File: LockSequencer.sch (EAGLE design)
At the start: 78 parts, among them IC1 4017D, IC2 NE555, K1 G2RATE-OJ, K2 G2RATE-OJ

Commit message: Nearly completed second revision
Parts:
- removed H2: MOUNT-HOLE2.8, holes:MOUNT-HOLE2.8
- added H3: MOUNT-PAD-ROUND2.8, holes:MOUNT-PAD-ROUND2.8
- H1: value MOUNT-HOLE2.8 -> MOUNT-PAD-ROUND2.8; device holes:MOUNT-HOLE2.8 -> holes:MOUNT-PAD-ROUND2.8
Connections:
- net N$27: now also K11.1; no longer K11.2
- net VSUPPLY: now also K11.2; no longer K11.1
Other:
- moved on the sheet: H1, K1
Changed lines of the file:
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@@
 <part name="JP7" library="pinhead" deviceset="PINHD-1X2" device=""/>
 <part name="JP8" library="pinhead" deviceset="PINHD-1X2" device=""/>
-<part name="H1" library="holes" deviceset="MOUNT-HOLE" device="2.8" value="MOUNT-HOLE2.8"/>
-<part name="H2" library="holes" deviceset="MOUNT-HOLE" device="2.8" value="MOUNT-HOLE2.8"/>
+<part name="H3" library="holes" deviceset="MOUNT-PAD-ROUND" device="2.8"/>
+<part name="H1" library="holes" deviceset="MOUNT-PAD-ROUND" device="2.8"/>
 </parts>
 <sheets>
@@
 <instance part="R4" gate="G$1" x="203.2" y="167.64" rot="R90"/>
 <instance part="T1" gate="G$1" x="223.52" y="20.32"/>
-<instance part="K1" gate="1" x="330.2" y="114.3"/>
+<instance part="K1" gate="1" x="330.2" y="114.3" rot="R180"/>
 <instance part="K1" gate="2" x="342.9" y="129.54"/>
 <instance part="D6" gate="G$1" x="378.46" y="127" rot="R180"/>
@@
 <instance part="JP7" gate="G$1" x="251.46" y="53.34" rot="R180"/>
 <instance part="JP8" gate="G$1" x="251.46" y="45.72" rot="R180"/>
-<instance part="H1" gate="G$1" x="302.26" y="165.1"/>
-<instance part="H2" gate="G$1" x="330.2" y="165.1"/>
+<instance part="H3" gate="G$1" x="309.88" y="175.26"/>
+<instance part="H1" gate="G$1" x="309.88" y="167.64"/>
 </instances>
 <busses>
@@
 </segment>
 <segment>
-<pinref part="K1" gate="1" pin="1"/>
-<wire x1="330.2" y1="127" x2="330.2" y2="119.38" width="0.1524" layer="91"/>
 <wire x1="330.2" y1="127" x2="320.04" y2="127" width="0.1524" layer="91"/>
 <pinref part="D1" gate="1" pin="2"/>
@@
 <wire x1="312.42" y1="124.46" x2="312.42" y2="127" width="0.1524" layer="91"/>
 <junction x="312.42" y="127"/>
+<pinref part="K1" gate="1" pin="2"/>
+<wire x1="330.2" y1="119.38" x2="330.2" y2="127" width="0.1524" layer="91"/>
 </segment>
 </net>
@@
 </segment>
 </net>
-<net name="VDD" class="1">
+<net name="VDD" class="3">
 <segment>
 <pinref part="R6" gate="G$1" pin="2"/>
@@
 <pinref part="T4" gate="G$1" pin="C"/>
 <wire x1="312.42" y1="99.06" x2="312.42" y2="101.6" width="0.1524" layer="91"/>
-<pinref part="K1" gate="1" pin="2"/>
-<wire x1="330.2" y1="109.22" x2="330.2" y2="101.6" width="0.1524" layer="91"/>
 <wire x1="330.2" y1="101.6" x2="320.04" y2="101.6" width="0.1524" layer="91"/>
 <pinref part="D1" gate="1" pin="1"/>
@@
 <wire x1="312.42" y1="104.14" x2="312.42" y2="101.6" width="0.1524" layer="91"/>
 <junction x="312.42" y="101.6"/>
-</segment>
-</net>
+<pinref part="K1" gate="1" pin="1"/>
+<wire x1="330.2" y1="109.22" x2="330.2" y2="101.6" width="0.1524" layer="91"/>
+</segment>
+</net>

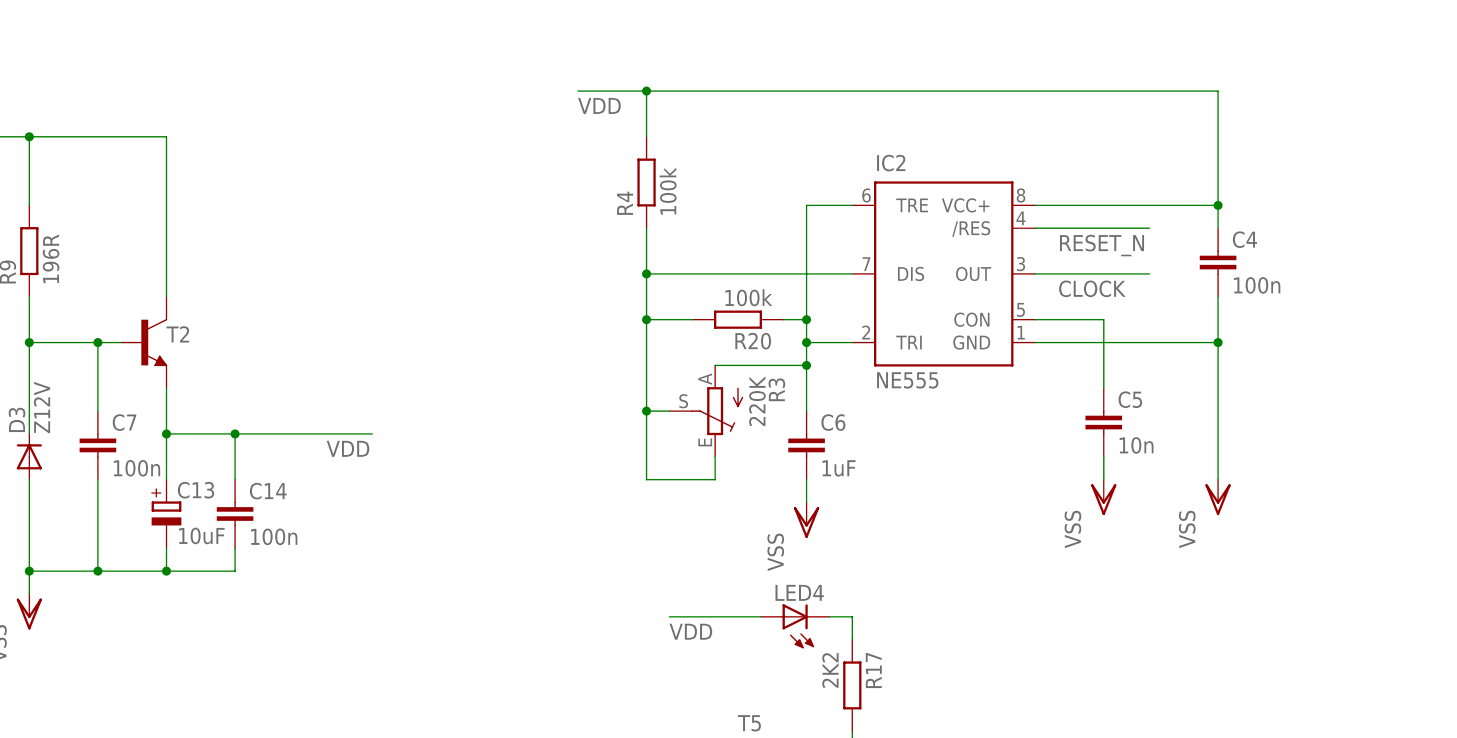
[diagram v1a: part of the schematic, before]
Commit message: Nearly finished on second revision - ground and power resrouted on right side of board. 4017 and 55 nearly done.
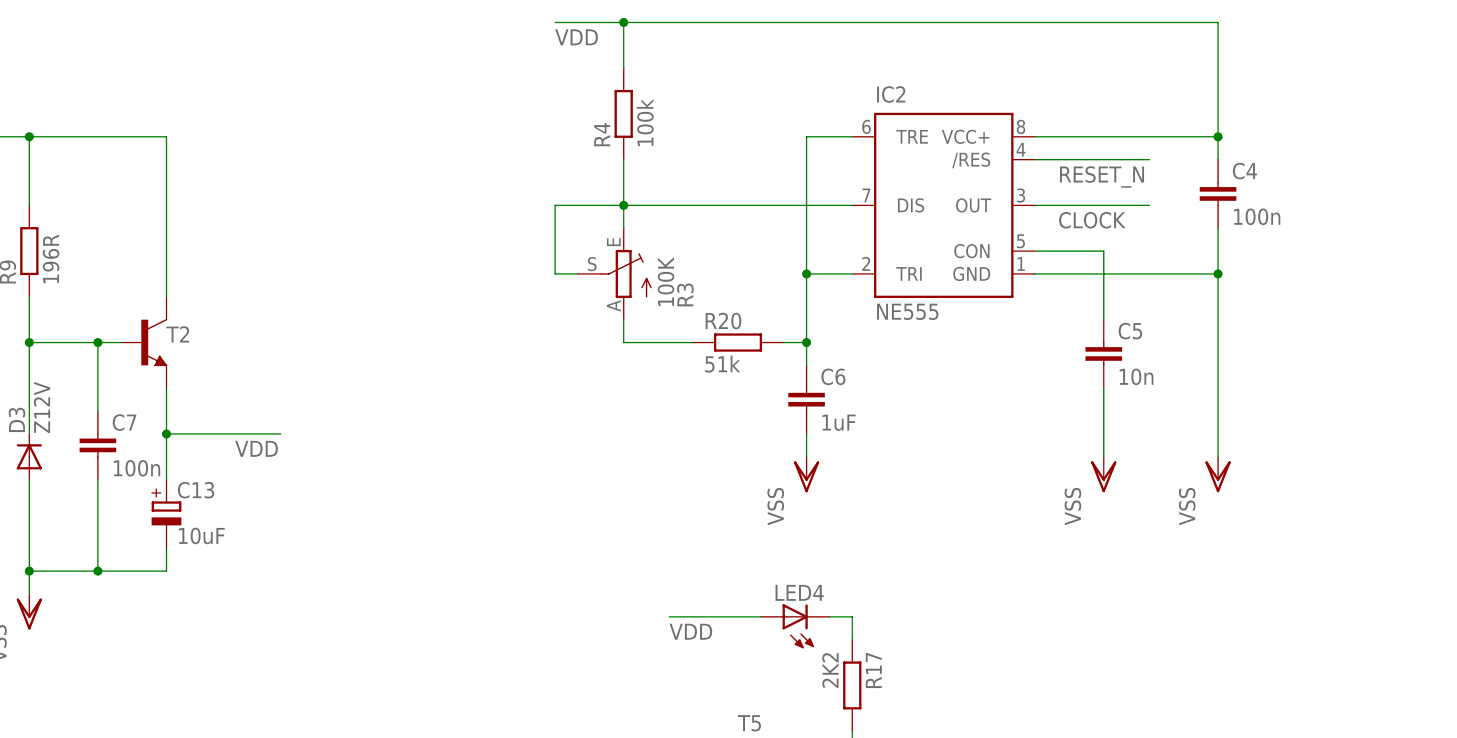
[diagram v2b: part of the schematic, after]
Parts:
- removed C14: 100n, rcl:C-EU050-024X044
- R17: device rcl:R-EU_0309/12 -> rcl:R-EU_0207/7
- R20: value 100k -> 51k
- R3: value 220K -> 100K
- R8: device rcl:R-EU_R0402 -> rcl:R-EU_0207/7
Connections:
- removed net N$24: IC2.DIS, R20.2, R3.E, R3.S, R4.1
- new net N$29: IC2.DIS, R3.E, R3.S, R4.1
- new net N$31: R20.1, R3.A
- net N$14: now also R20.2; no longer R20.1, R3.A
- net VDD: no longer C14.1
- net VSS: no longer C14.2
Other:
- moved on the sheet: C4, C5, C6, IC2, R20, R3, R4

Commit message: Second revision complete minus DRC
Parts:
- removed D6, D9: UF5404, diode:SCHOTTKY-DIODECB429-15
- added D4: (no value), diode:SCHOTTKY-DIODECB429-15VR
- added D5: (no value), diode:SCHOTTKY-DIODECB429-15V
- D1, D11, D2, D8: value P6KEXXC -> P6KEXXCTS-P6KE; device diode:P6KEXXC -> diode:P6KEXXCTS-P6KE
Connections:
- removed net N$39: D9.A, R19.2
- new net N$24: IC2.DIS, R3.A, R4.1
- net N$21: now also D4.C, D5.C, X5-1.KL; no longer D6.C, D9.C, X6-1.KL
- net N$29: now also D4.A, R18.2; no longer IC2.DIS, R3.E, R3.S, R4.1
- net N$30: now also X6-1.KL; no longer X5-1.KL
- net N$31: now also R3.E, R3.S; no longer R3.A
- net N$37: now also D5.A, R19.2; no longer D6.A, R18.2
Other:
- moved on the sheet: R3, X5-1, X6-1
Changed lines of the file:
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@@
 <part name="T1" library="transistor" deviceset="*-NPN_DRIVER-" device=""/>
 <part name="K1" library="relay" deviceset="G2RA" device="TE-OJ" value="G2RATE-OJ"/>
-<part name="D6" library="diode" deviceset="SCHOTTKY-DIODE" device="CB429-15" value="UF5404"/>
 <part name="D7" library="diode" deviceset="1N581*" device="" technology="9-T"/>
 <part name="C11" library="rcl" deviceset="C-EU" device="050-024X044" value="100n"/>
@@
 <part name="R12" library="rcl" deviceset="R-EU_" device="0207/7" value="2K2"/>
 <part name="T4" library="transistor" deviceset="*-NPN-" device="SOT23-BEC" technology="MMBTA42LT1"/>
-<part name="D1" library="diode" deviceset="P6KEXXC" device=""/>
+<part name="D1" library="diode" deviceset="P6KEXXC" device="TS-P6KE" value="P6KEXXCTS-P6KE"/>
 <part name="R11" library="rcl" deviceset="R-EU_" device="R0603" value="15K4"/>
 <part name="LED2" library="led" deviceset="LED" device="5MM"/>
 <part name="R13" library="rcl" deviceset="R-EU_" device="0207/7" value="15K4"/>
 <part name="T3" library="transistor" deviceset="*-NPN-" device="SOT23-BEC" technology="MMBTA42LT1"/>
-<part name="D2" library="diode" deviceset="P6KEXXC" device=""/>
+<part name="D2" library="diode" deviceset="P6KEXXC" device="TS-P6KE" value="P6KEXXCTS-P6KE"/>
 <part name="R14" library="rcl" deviceset="R-EU_" device="R0603" value="15K4"/>
 <part name="LED3" library="led" deviceset="LED" device="5MM"/>
@@
 <part name="X5" library="con-wago-500" deviceset="W237-102" device=""/>
 <part name="X6" library="con-wago-500" deviceset="W237-102" device=""/>
-<part name="D8" library="diode" deviceset="P6KEXXC" device=""/>
+<part name="D8" library="diode" deviceset="P6KEXXC" device="TS-P6KE" value="P6KEXXCTS-P6KE"/>
 <part name="F3" library="fuse" deviceset="TE5" device=""/>
 <part name="F4" library="fuse" deviceset="TE5" device=""/>
-<part name="D9" library="diode" deviceset="SCHOTTKY-DIODE" device="CB429-15" value="UF5404"/>
 <part name="R18" library="rcl" deviceset="R-EU_" device="R2512" value="0R1"/>
 <part name="R19" library="rcl" deviceset="R-EU_" device="R2512" value="0R1"/>
@@
 <part name="X8" library="con-wago-500" deviceset="W237-102" device=""/>
 <part name="X9" library="con-wago-500" deviceset="W237-102" device=""/>
-<part name="D11" library="diode" deviceset="P6KEXXC" device=""/>
+<part name="D11" library="diode" deviceset="P6KEXXC" device="TS-P6KE" value="P6KEXXCTS-P6KE"/>
 <part name="F5" library="fuse" deviceset="TE5" device=""/>
 <part name="F6" library="fuse" deviceset="TE5" device=""/>
@@
 <part name="H3" library="holes" deviceset="MOUNT-PAD-ROUND" device="2.8"/>
 <part name="H1" library="holes" deviceset="MOUNT-PAD-ROUND" device="2.8"/>
+<part name="D4" library="diode" deviceset="SCHOTTKY-DIODE" device="CB429-15VR"/>
+<part name="D5" library="diode" deviceset="SCHOTTKY-DIODE" device="CB429-15V"/>
 </parts>
 <sheets>
@@
 <instance part="K1" gate="1" x="330.2" y="114.3" rot="R180"/>
 <instance part="K1" gate="2" x="342.9" y="129.54"/>
-<instance part="D6" gate="G$1" x="378.46" y="127" rot="R180"/>
 <instance part="D7" gate="G$1" x="43.18" y="154.94"/>
 <instance part="C11" gate="G$1" x="60.96" y="149.86"/>
@@
 <instance part="C6" gate="G$1" x="220.98" y="144.78"/>
 <instance part="C4" gate="G$1" x="266.7" y="167.64"/>
-<instance part="R3" gate="1" x="200.66" y="157.48" rot="MR0"/>
+<instance part="R3" gate="1" x="200.66" y="160.02" rot="MR180"/>
 <instance part="C13" gate="G$1" x="149.86" y="132.08"/>
 <instance part="D3" gate="G$1" x="134.62" y="137.16" rot="R90"/>
@@
 <instance part="K2" gate="1" x="330.2" y="66.04" rot="R180"/>
 <instance part="K2" gate="2" x="347.98" y="73.66" rot="R180"/>
-<instance part="X5" gate="-1" x="350.52" y="109.22" rot="R180"/>
+<instance part="X5" gate="-1" x="363.22" y="111.76" rot="R180"/>
 <instance part="X5" gate="-2" x="350.52" y="111.76" rot="R180"/>
-<instance part="X6" gate="-1" x="363.22" y="111.76" rot="R180"/>
+<instance part="X6" gate="-1" x="350.52" y="109.22" rot="R180"/>
 <instance part="X6" gate="-2" x="363.22" y="109.22" rot="R180"/>
 <instance part="D8" gate="1" x="370.84" y="104.14" rot="R90"/>
 <instance part="F3" gate="1" x="355.6" y="101.6" rot="R90"/>
 <instance part="F4" gate="1" x="342.9" y="101.6" rot="R90"/>
-<instance part="D9" gate="G$1" x="378.46" y="119.38" rot="R180"/>
 <instance part="R18" gate="G$1" x="388.62" y="127" rot="R180"/>
 <instance part="R19" gate="G$1" x="388.62" y="119.38" rot="R180"/>
@@
 <instance part="H3" gate="G$1" x="309.88" y="175.26"/>
 <instance part="H1" gate="G$1" x="309.88" y="167.64"/>
+<instance part="D4" gate="G$1" x="378.46" y="127" rot="R180"/>
+<instance part="D5" gate="G$1" x="378.46" y="119.38" rot="R180"/>
 </instances>
 <busses>
@@
 <wire x1="355.6" y1="119.38" x2="370.84" y2="119.38" width="0.1524" layer="91"/>
 <wire x1="370.84" y1="109.22" x2="370.84" y2="119.38" width="0.1524" layer="91"/>
-<pinref part="D9" gate="G$1" pin="C"/>
-<wire x1="375.92" y1="119.38" x2="370.84" y2="119.38" width="0.1524" layer="91"/>
 <junction x="370.84" y="119.38"/>
-<pinref part="D6" gate="G$1" pin="C"/>
-<wire x1="375.92" y1="127" x2="370.84" y2="127" width="0.1524" layer="91"/>
 <wire x1="370.84" y1="127" x2="370.84" y2="119.38" width="0.1524" layer="91"/>
 <pinref part="K1" gate="2" pin="P"/>
 <wire x1="342.9" y1="124.46" x2="342.9" y2="119.38" width="0.1524" layer="91"/>
 <junction x="342.9" y="119.38"/>
-<pinref part="X6" gate="-1" pin="KL"/>
-<wire x1="358.14" y1="111.76" x2="355.6" y2="111.76" width="0.1524" layer="91"/>
 <wire x1="355.6" y1="111.76" x2="355.6" y2="119.38" width="0.1524" layer="91"/>
 <junction x="355.6" y="119.38"/>
 <pinref part="X5" gate="-2" pin="KL"/>
 <wire x1="345.44" y1="111.76" x2="342.9" y2="111.76" width="0.1524" layer="91"/>
+<pinref part="X5" gate="-1" pin="KL"/>
+<wire x1="358.14" y1="111.76" x2="355.6" y2="111.76" width="0.1524" layer="91"/>
+<pinref part="D4" gate="G$1" pin="C"/>
+<wire x1="375.92" y1="127" x2="370.84" y2="127" width="0.1524" layer="91"/>
+<pinref part="D5" gate="G$1" pin="C"/>
+<wire x1="375.92" y1="119.38" x2="370.84" y2="119.38" width="0.1524" layer="91"/>
 </segment>
 </net>
@@
 <pinref part="F4" gate="1" pin="2"/>
 <wire x1="342.9" y1="106.68" x2="342.9" y2="109.22" width="0.1524" layer="91"/>
-<pinref part="X5" gate="-1" pin="KL"/>
+<pinref part="X6" gate="-1" pin="KL"/>
 <wire x1="345.44" y1="109.22" x2="342.9" y2="109.22" width="0.1524" layer="91"/>
-</segment>
-</net>
-<net name="N$37" class="0">
-<segment>
-<pinref part="D6" gate="G$1" pin="A"/>
-<wire x1="381" y1="127" x2="383.54" y2="127" width="0.1524" layer="91"/>
-<pinref part="R18" gate="G$1" pin="2"/>
-</segment>
-</net>
-<net name="N$39" class="0">
-<segment>
-<pinref part="D9" gate="G$1" pin="A"/>
-<wire x1="381" y1="119.38" x2="383.54" y2="119.38" width="0.1524" layer="91"/>
-<pinref part="R19" gate="G$1" pin="2"/>
 </segment>
 </net>
@@
 </segment>
 </net>
-<net name="N$29" class="0">
-<segment>
-<wire x1="193.04" y1="157.48" x2="193.04" y2="165.1" width="0.1524" layer="91"/>
-<wire x1="193.04" y1="165.1" x2="200.66" y2="165.1" width="0.1524" layer="91"/>
+<net name="N$31" class="0">
+<segment>
+<pinref part="R20" gate="G$1" pin="1"/>
+<wire x1="208.28" y1="149.86" x2="200.66" y2="149.86" width="0.1524" layer="91"/>
+<wire x1="208.28" y1="160.02" x2="208.28" y2="152.4" width="0.1524" layer="91"/>
+<wire x1="208.28" y1="152.4" x2="200.66" y2="152.4" width="0.1524" layer="91"/>
+<pinref part="R3" gate="1" pin="S"/>
+<wire x1="208.28" y1="160.02" x2="205.74" y2="160.02" width="0.1524" layer="91"/>
+<wire x1="200.66" y1="149.86" x2="200.66" y2="152.4" width="0.1524" layer="91"/>
 <pinref part="R3" gate="1" pin="E"/>
-<wire x1="200.66" y1="162.56" x2="200.66" y2="165.1" width="0.1524" layer="91"/>
-<pinref part="R3" gate="1" pin="S"/>
-<wire x1="193.04" y1="157.48" x2="195.58" y2="157.48" width="0.1524" layer="91"/>
+<wire x1="200.66" y1="152.4" x2="200.66" y2="154.94" width="0.1524" layer="91"/>
+<junction x="200.66" y="152.4"/>
+</segment>
+</net>
+<net name="N$24" class="0">
+<segment>
+<pinref part="IC2" gate="G$1" pin="DIS"/>
+<pinref part="R3" gate="1" pin="A"/>
+<wire x1="226.06" y1="165.1" x2="200.66" y2="165.1" width="0.1524" layer="91"/>
 <pinref part="R4" gate="G$1" pin="1"/>
 <wire x1="200.66" y1="170.18" x2="200.66" y2="165.1" width="0.1524" layer="91"/>
 <junction x="200.66" y="165.1"/>
-<pinref part="IC2" gate="G$1" pin="DIS"/>
-<wire x1="226.06" y1="165.1" x2="200.66" y2="165.1" width="0.1524" layer="91"/>
-</segment>
-</net>
-<net name="N$31" class="0">
-<segment>
-<pinref part="R20" gate="G$1" pin="1"/>
-<wire x1="208.28" y1="149.86" x2="200.66" y2="149.86" width="0.1524" layer="91"/>
-<pinref part="R3" gate="1" pin="A"/>
-<wire x1="200.66" y1="149.86" x2="200.66" y2="152.4" width="0.1524" layer="91"/>
-</segment>
-</net>
+</segment>
+</net>
+<net name="N$29" class="0">
+<segment>
+<pinref part="R18" gate="G$1" pin="2"/>
+<pinref part="D4" gate="G$1" pin="A"/>
+<wire x1="383.54" y1="127" x2="381" y2="127" width="0.1524" layer="91"/>
+</segment>
+</net>
+<net name="N$37" class="0">
+<segment>
+<pinref part="R19" gate="G$1" pin="2"/>
+<pinref part="D5" gate="G$1" pin="A"/>
+<wire x1="383.54" y1="119.38" x2="381" y2="119.38" width="0.1524" layer="91"/>
+</segment>
+</net>

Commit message: Completed tweaks to second revision including new package for 1N5819. Ready for printing.
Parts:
- removed D7: 1N5819-T, diode:1N5819-T
- removed H1, H3: MOUNT-PAD-ROUND2.8, holes:MOUNT-PAD-ROUND2.8
- added D6: P6KEXXCTS-P6KE, diode:P6KEXXCTS-P6KE
- added D9: (no value), diode:DIODE-SOD123
- D4, D5: value (none) -> UF5404
- R13: value 15K4 -> 2K2
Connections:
- removed net N$19: D7.A, F1.1
- new net VEXTERNAL-FUSED: D6.2, D9.A, F1.1
- net VSS: now also D6.1
- net VSUPPLY: now also D9.C; no longer D7.C
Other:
- moved on the sheet: C1, C11

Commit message: Extra revision following minor assembly problems
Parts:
- R3: value 100K -> 220K
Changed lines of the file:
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@@
 <part name="C6" library="rcl" deviceset="C-EU" device="C1206K" value="1uF"/>
 <part name="C4" library="rcl" deviceset="C-EU" device="050-024X044" value="100n"/>
-<part name="R3" library="pot" deviceset="TRIM_EU-" device="CA9V" value="100K"/>
+<part name="R3" library="pot" deviceset="TRIM_EU-" device="CA9V" value="220K"/>
 <part name="C13" library="rcl" deviceset="CPOL-EU" device="E2-5" value="10uF"/>
 <part name="D3" library="diode" deviceset="DIODE-" device="SOD323-W" value="Z12V"/>
